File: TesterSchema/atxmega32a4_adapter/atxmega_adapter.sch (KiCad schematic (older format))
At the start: 23 parts, among them IC1 ATXMEGA32A4-M, P1 DIL40, Q1 BC817-40, Q2 BC817-40, Q3 BC817-40, U1 APE8865N-33-HF-3

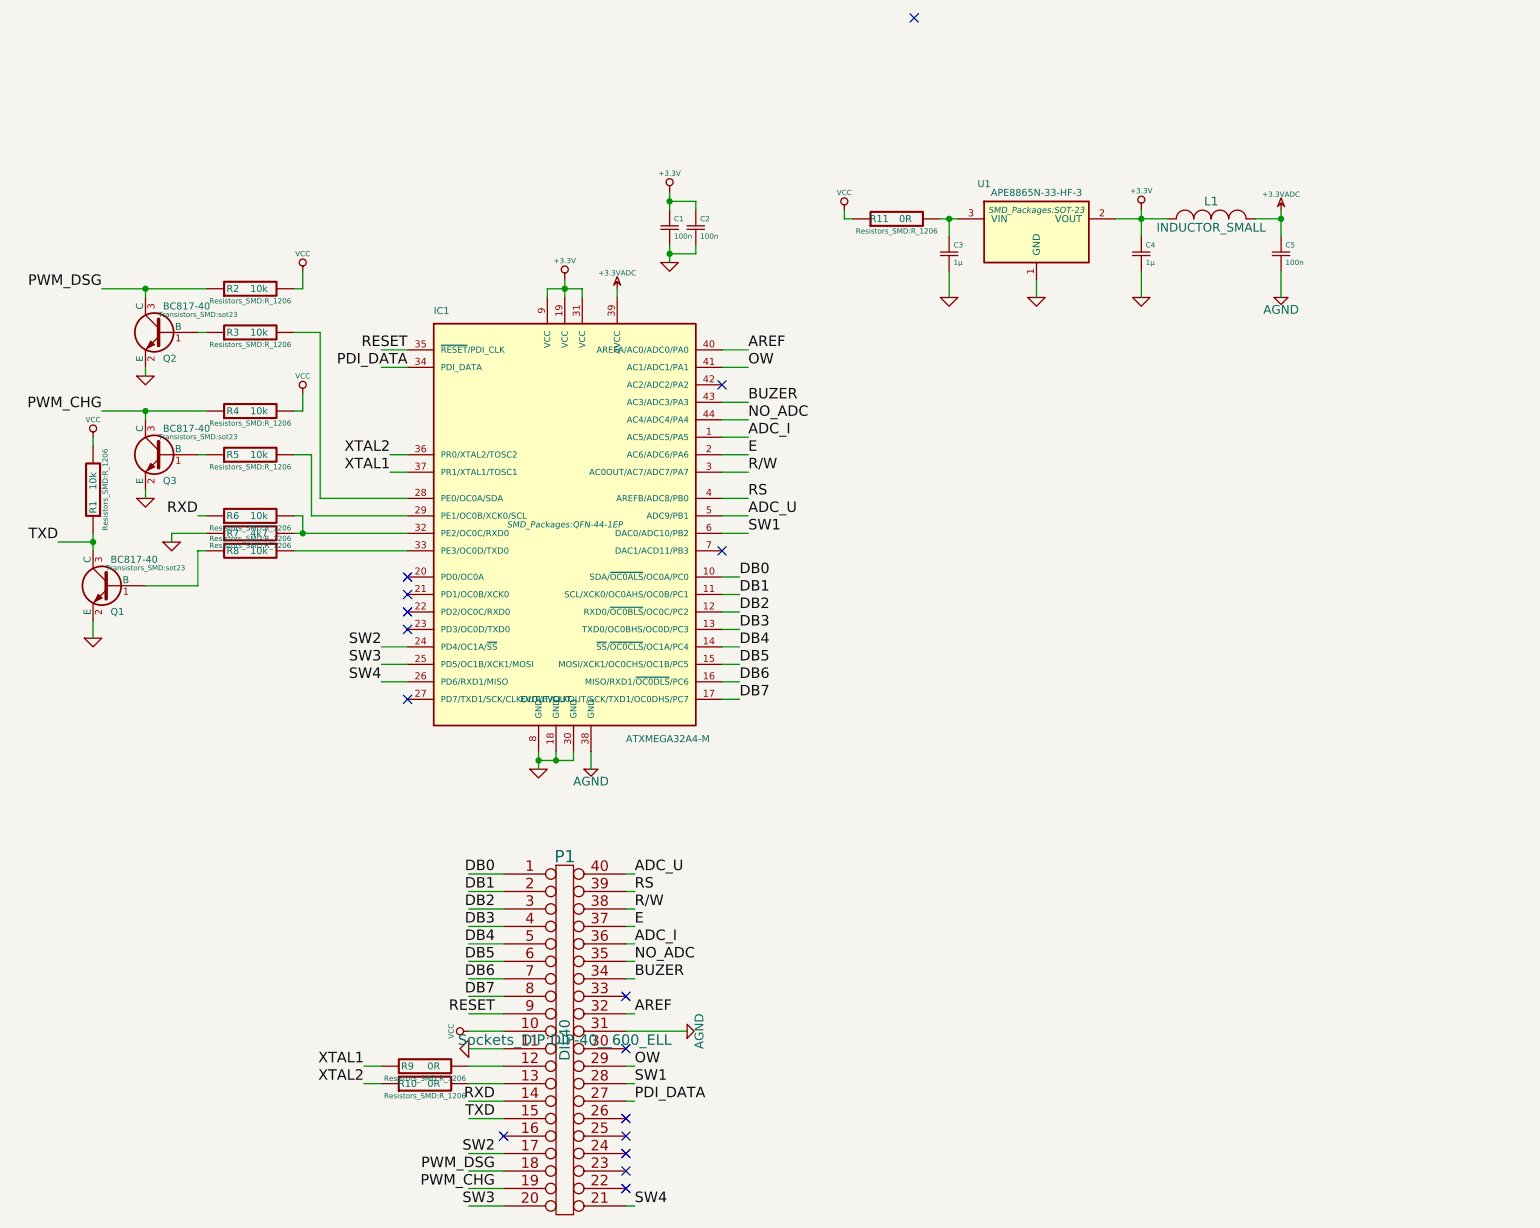
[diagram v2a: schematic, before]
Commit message: Dodanie diody sygnalizującej zasilanie i 2 diodek pomocniczych
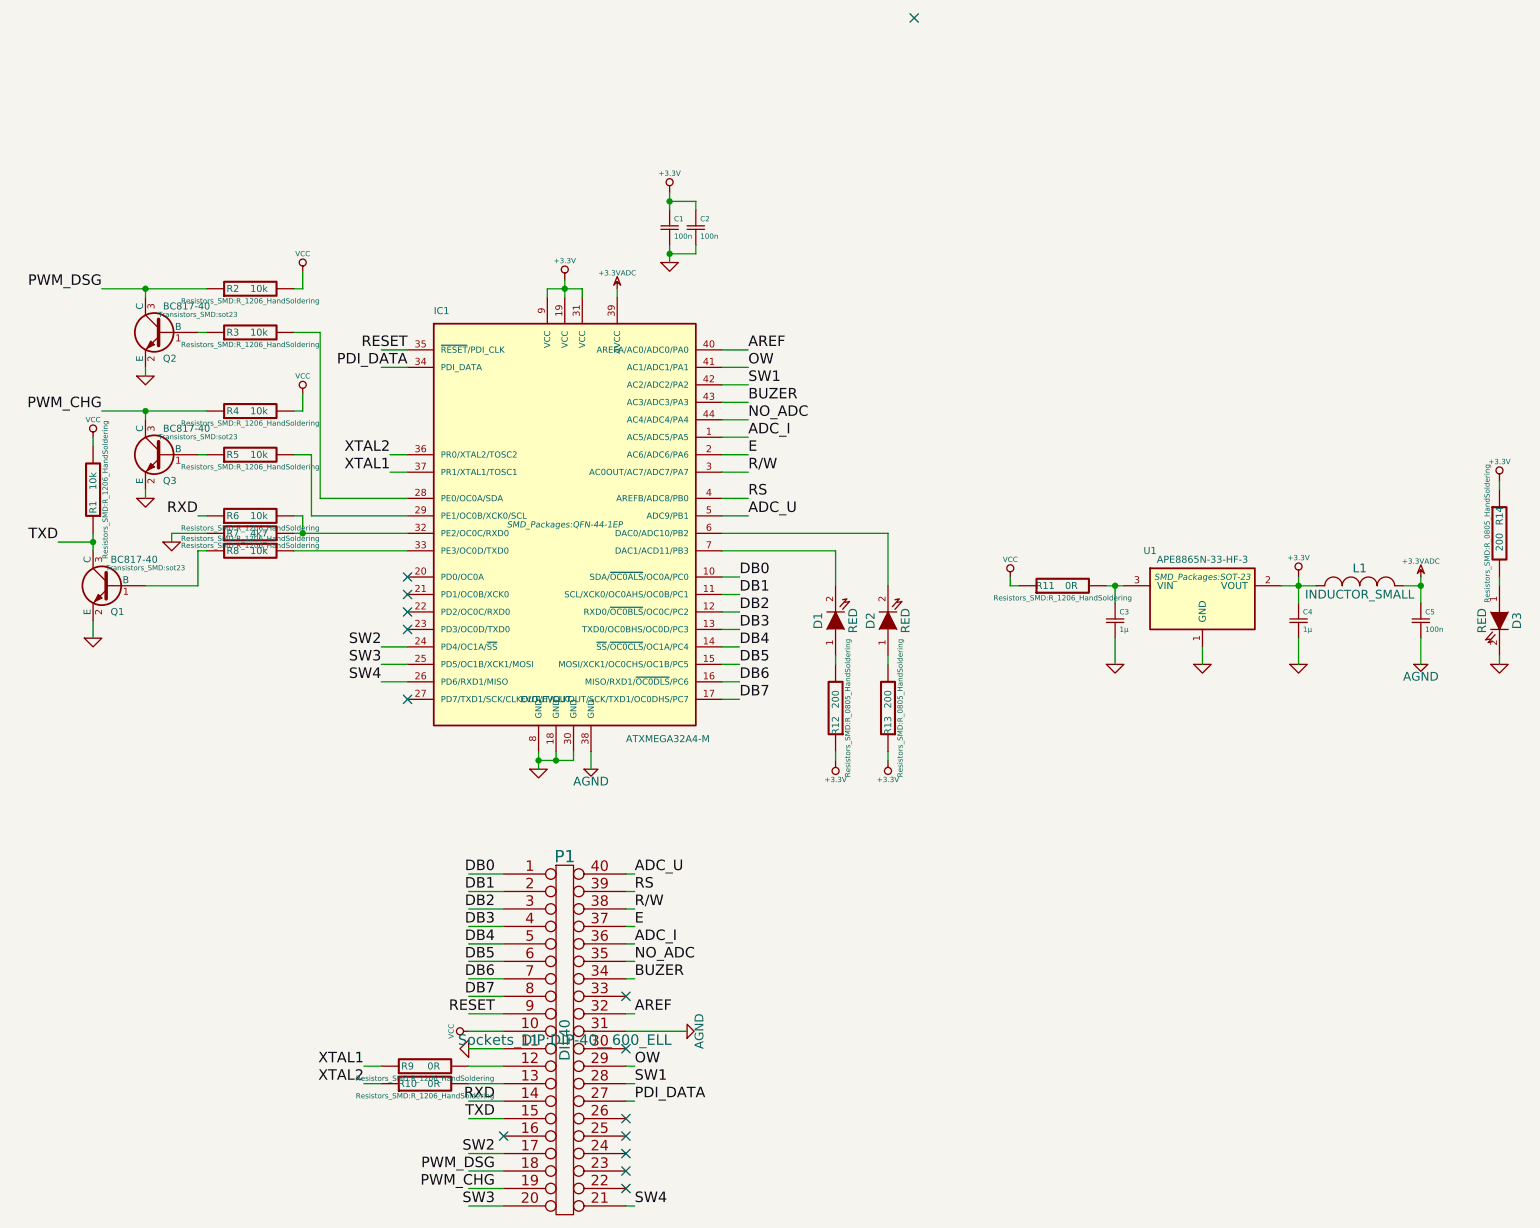
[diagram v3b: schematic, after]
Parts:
- added D1, D2, D3: RED, LEDs:LED-0805, symbol LED
- added R12, R13, R14: 200, Resistors_SMD:R_0805_HandSoldering, symbol R
- R1, R10, R11, R2, R3, R4, R5, R6, R7, R8, R9: footprint Resistors_SMD:R_1206 -> Resistors_SMD:R_1206_HandSoldering
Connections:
- wire segments 133 -> 130
- no-connect marks 16 -> 14
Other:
- moved on the sheet: C3, C4, C5, L1, R11, U1

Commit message: Zmiana nazwy stabilizatore/ poprawki w adapeerze
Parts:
- U1: value APE8865N-33-HF-3 -> MCP1702T3302ECB
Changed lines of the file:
@@
-	1    0    0    -1
-$EndComp
-$Comp
-L APE8865N-33-HF-3 U1
-U 1 1 54D1474B
-P 8150 2950
-F 0 "U1" H 7850 3200 40  0000 C CNN
-F 1 "APE8865N-33-HF-3" H 8150 3150 40  0000 C CNN
-F 2 "SMD_Packages:SOT-23" H 8150 3050 35  0000 C CIN
-F 3 "" H 8150 2950 60  0000 C CNN
-	1    8150 2950
 	1    0    0    -1
 $EndComp
@@
 NoConn ~ 3600 2950
 NoConn ~ 3600 2850
+$Comp
+L APE8865N-33-HF-3 U1
+U 1 1 54D1474B
+P 8150 2950
+F 0 "U1" H 7850 3200 40  0000 C CNN
+F 1 "MCP1702T3302ECB" H 8150 3150 40  0000 C CNN
+F 2 "SMD_Packages:SOT-23" H 8150 3050 35  0000 C CIN
+F 3 "" H 8150 2950 60  0000 C CNN
+	1    8150 2950
+	1    0    0    -1
+$EndComp
 $EndSCHEMATC
